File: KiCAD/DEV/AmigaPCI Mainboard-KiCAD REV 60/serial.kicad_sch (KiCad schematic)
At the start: 29 parts, among them CN203 DB25_Stack_FemaleAndMale, Q200 MMBT3904, Q201 MMBT3906, U203 8520, U205 TRS213, U209 74HCT08

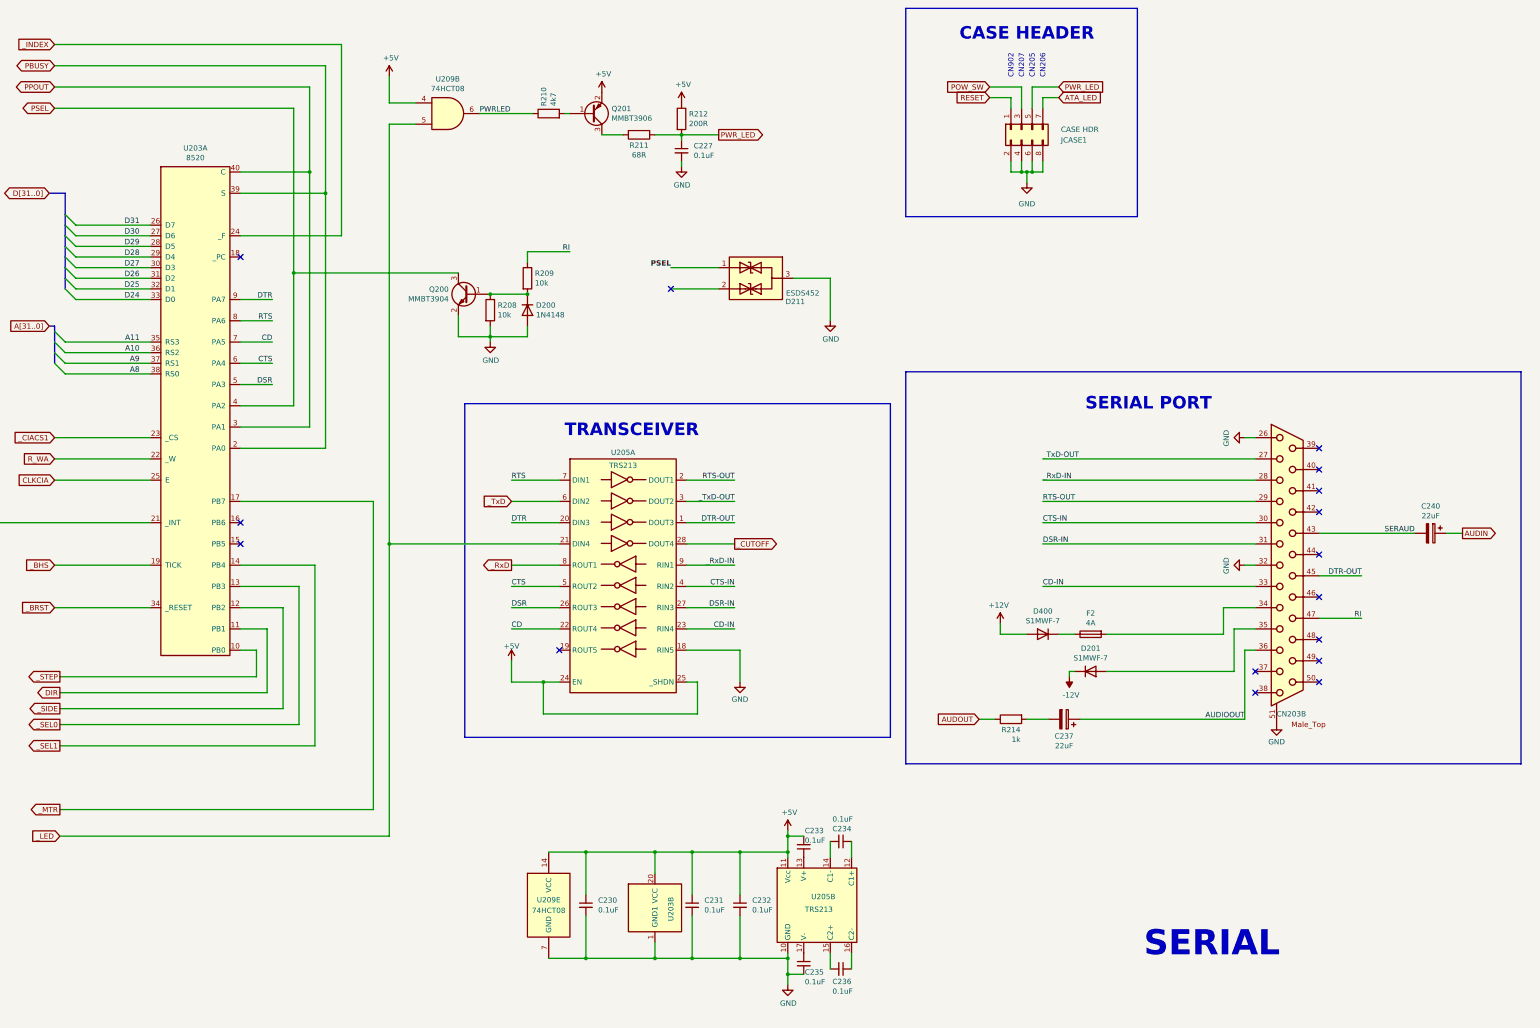
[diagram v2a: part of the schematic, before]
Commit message: APCI Rev 6.0 work.
Replace TS213 with AZ75232 serial driver to fix audio filter issue.
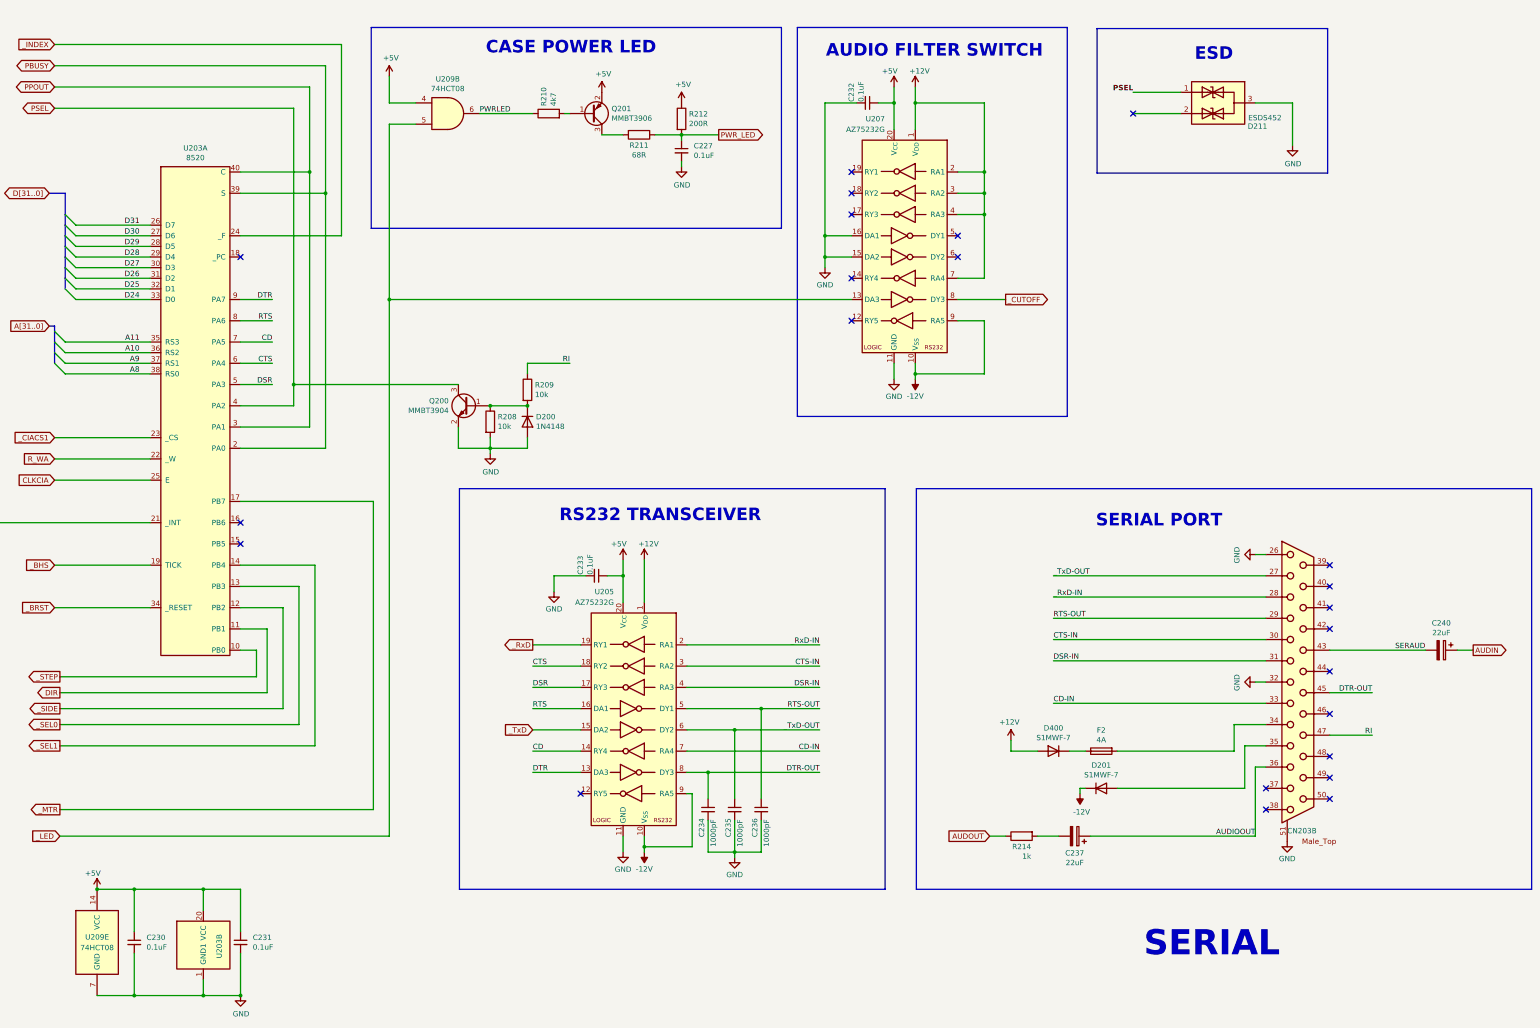
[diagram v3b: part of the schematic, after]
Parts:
- removed JCASE1: CASE HDR, Connector_PinHeader_2.54mm:PinHeader_2x04_P2.54mm_Vertical, symbol Connector_Generic:Conn_02x04_Odd_Even
- removed U205: TRS213, Package_SO:SSOP-28_5.3x10.2mm_P0.65mm, symbol AmigaPCI-Symbols:TRS213
- added U205, U207: AZ75232G, Package_SO:TSSOP-20_4.4x6.5mm_P0.65mm, symbol Interface_UART:AZ75232G
- C234, C235, C236: value 0.1uF -> 1000pF
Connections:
- net +12V: now also U205.1 (V_{DD}), U207.1 (V_{DD}), U207.2 (RA1), U207.3 (RA2), U207.4 (RA3), U207.7 (RA4)
- net +5V: now also C233.1, U205.20 (V_{CC}), U207.20 (V_{CC}); no longer C233.2
- net -12V: now also U205.10 (V_{SS}), U205.9 (RA5), U207.10 (V_{SS}), U207.9 (RA5)
- net CD: now also U205.14 (RY4)
- net CD-IN: now also U205.7 (RA4)
- net CTS: now also U205.18 (RY2)
- net CTS-IN: now also U205.3 (RA2)
- net DSR: now also U205.17 (RY3)
- net DSR-IN: now also U205.4 (RA3)
- net DTR: now also U205.13 (DA3)
- net DTR-OUT: now also C234.1, U205.8 (DY3)
- net GND: now also C233.2, C234.2, C236.2, U205.11 (GND), U207.11 (GND), U207.15 (DA2), U207.16 (DA1)
- net RTS: now also U205.16 (DA1)
- net RTS-OUT: now also C236.1, U205.5 (DY1)
- net _CUTOFF: now also U207.8 (DY3)
- net _LED: now also U207.13 (DA3)
- net _RxD: now also U205.19 (RY1)
- net _RxD-IN: now also U205.2 (RA1)
- net _TxD: now also U205.15 (DA2)
- net _TxD-OUT: now also C235.1, U205.6 (DY2)
- no-connect marks 16 -> 23
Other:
- note added: "AUDIO FILTER SWITCH"
- note added: "CASE POWER LED"
- note added: "ESD"
- note added: "RS232 TRANSCEIVER"
- note removed: "CASE HEADER"
- note removed: "CN205"
- note removed: "CN206"
- note removed: "CN207"
- note removed: "CN902"
- note removed: "TRANSCEIVER"
- moved on the sheet: C230, C231, C233, C234, C237, C240, CN203B, D200, D201, D211, D400, F2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
